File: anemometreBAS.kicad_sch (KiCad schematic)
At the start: 15 parts, among them U1 TP4056

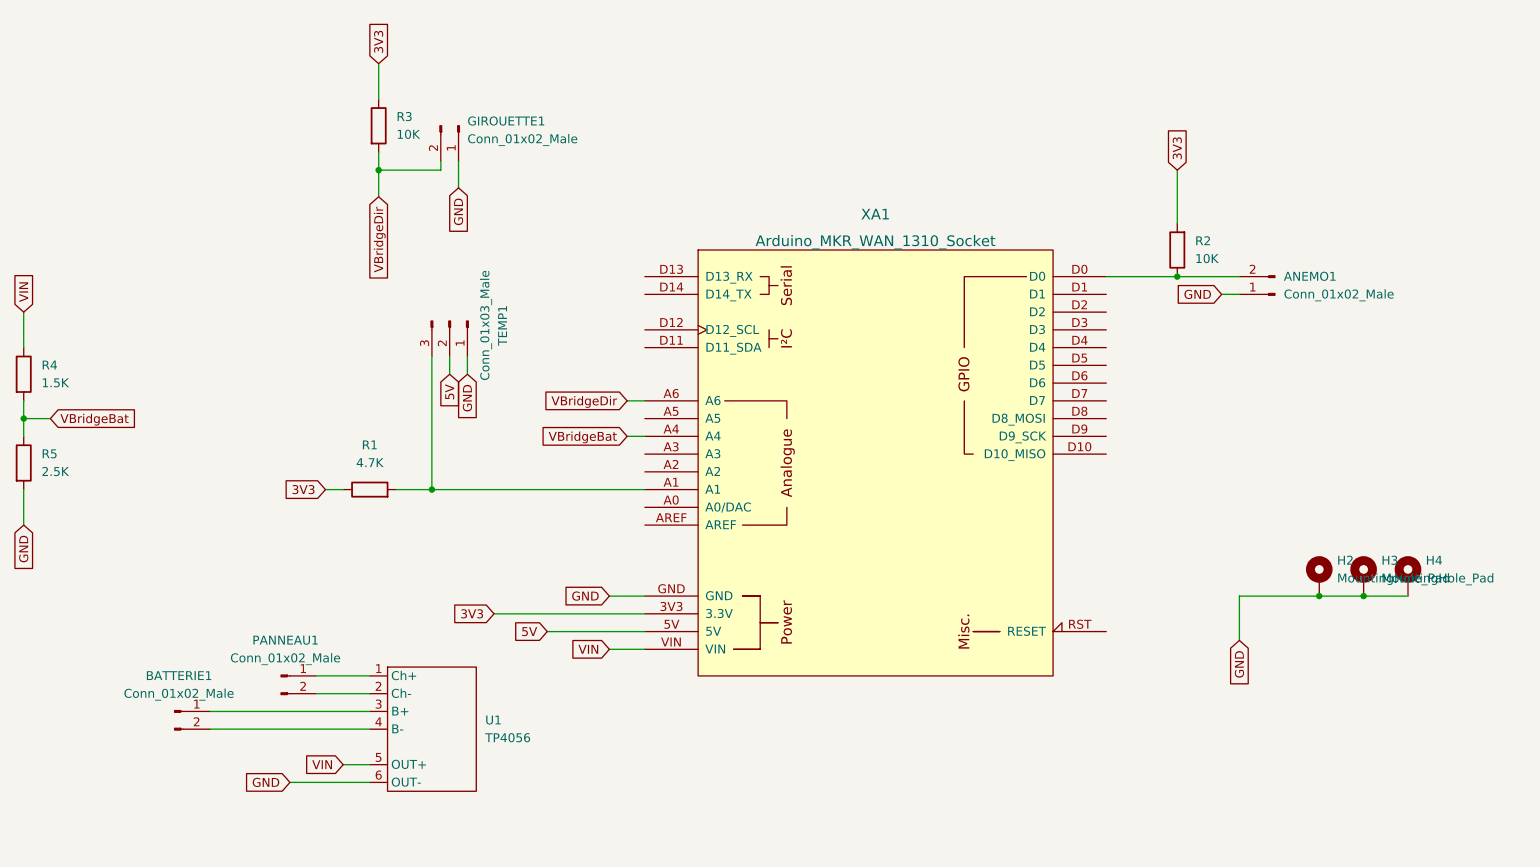
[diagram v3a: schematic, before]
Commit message: adding optionnal CEM schottky diode MKR 3D model update
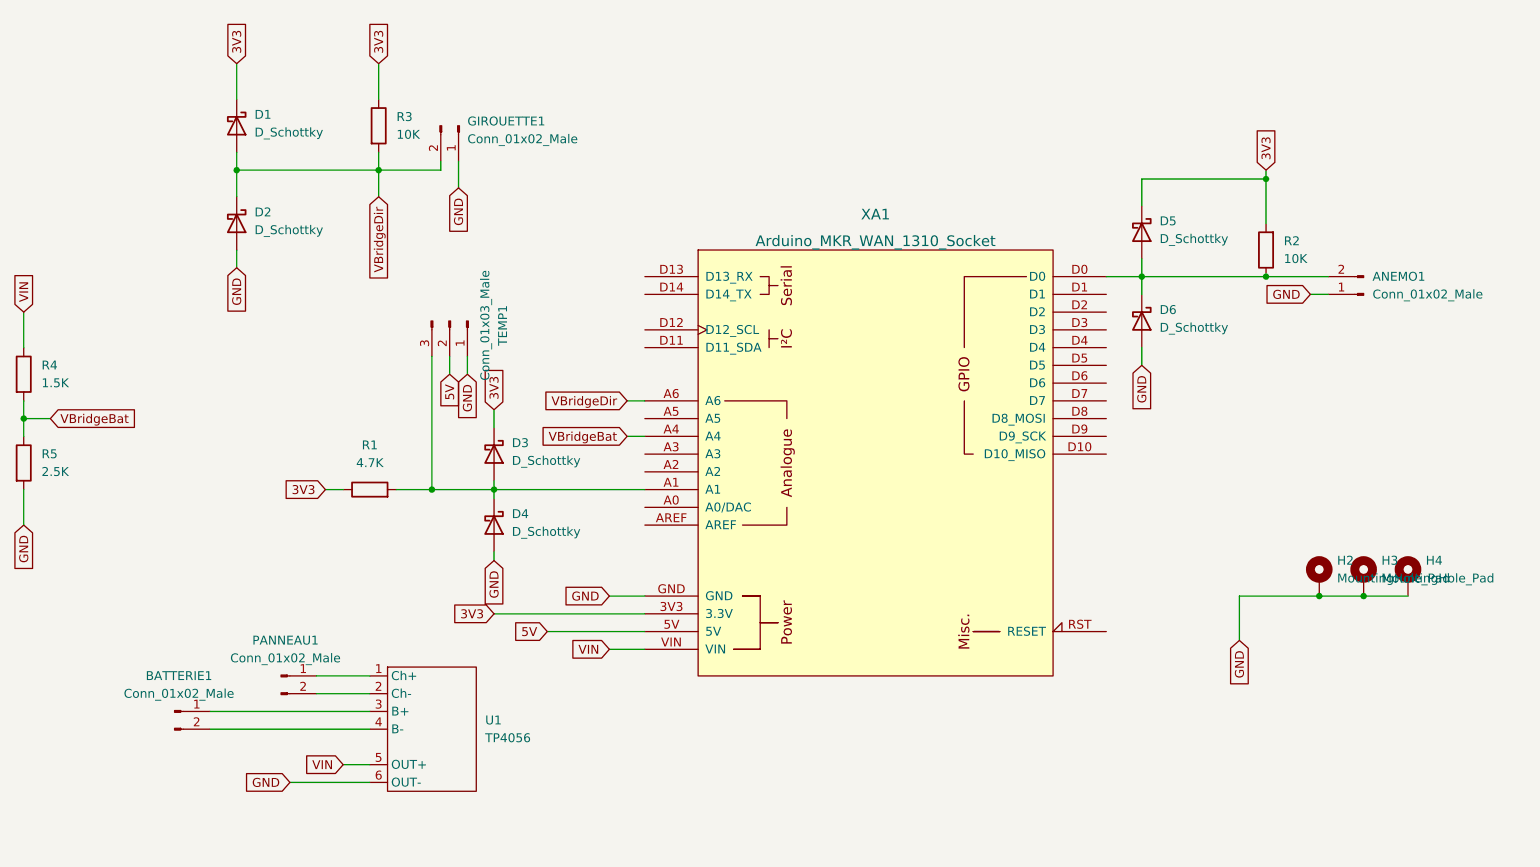
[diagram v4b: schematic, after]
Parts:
- added D1, D2, D3, D4, D5, D6: D_Schottky, Diode_THT:D_DO-35_SOD27_P7.62mm_Horizontal, symbol Device:D_Schottky
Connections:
- net 3V3: now also D1.1 (K), D3.1 (K), D5.1 (K)
- net GND: now also D2.2 (A), D4.2 (A), D6.2 (A)
- net VBridgeDir: now also D1.2 (A), D2.1 (K)
- net at R1.2, TEMP1.3 (Pin_3), XA1.A1: now also D3.2 (A), D4.1 (K)
- net at ANEMO1.2 (Pin_2), R2.1, XA1.D0: now also D5.2 (A), D6.1 (K)
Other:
- moved on the sheet: ANEMO1, R2

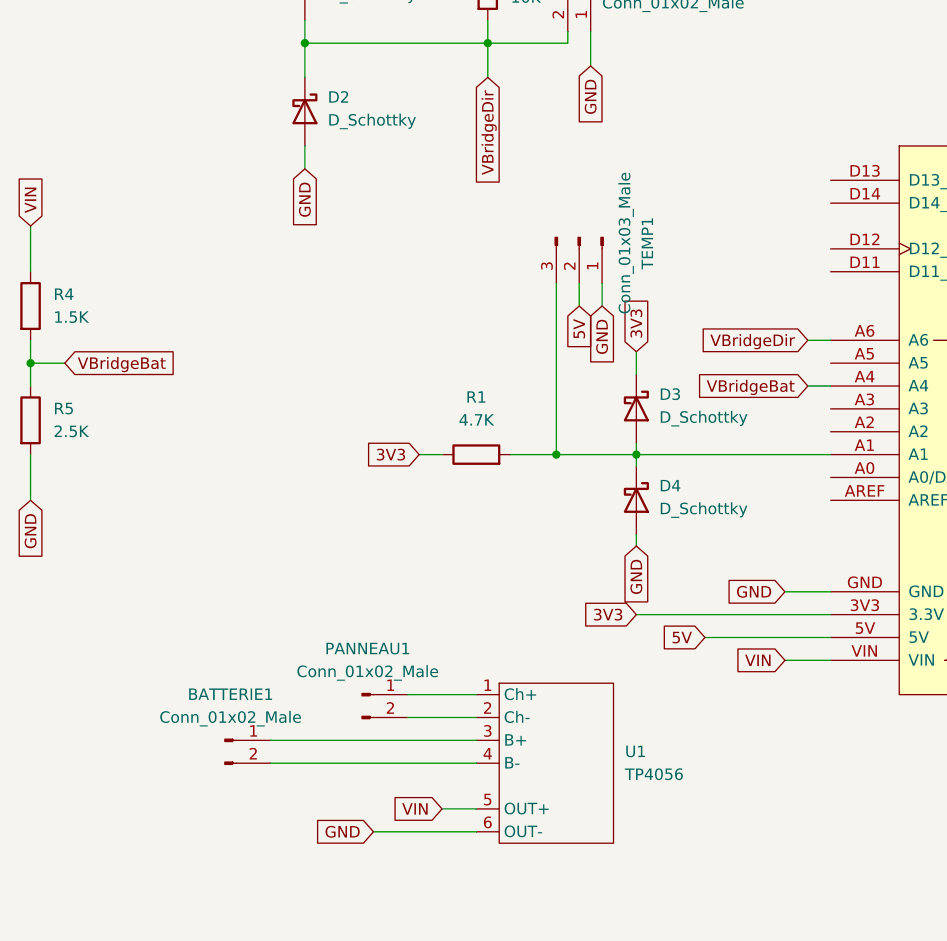
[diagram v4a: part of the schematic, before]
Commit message: Corrections alim (#2)
* Fix power issue

* add power connector as jst
routing pcb

---------

Co-authored-by: sdaviet <sylvain.daviet@gmail.com>
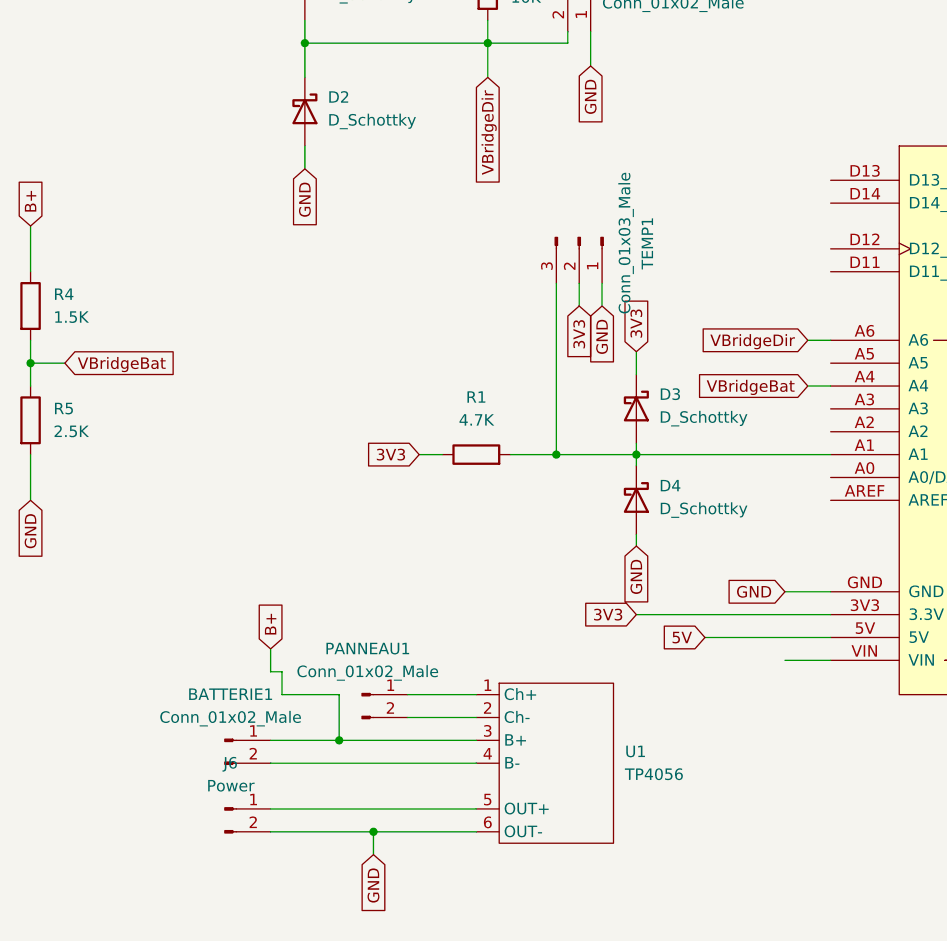
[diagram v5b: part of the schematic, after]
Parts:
- added J6: Power, Connector_JST:JST_XH_B2B-XH-A_1x02_P2.50mm_Vertical, symbol Connector:Conn_01x02_Male
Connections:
- net 3V3: now also TEMP1.2 (Pin_2)
- net 5V: no longer TEMP1.2 (Pin_2)
- net GND: now also J6.2 (Pin_2)
- net B+: now reaches BATTERIE1.1 (Pin_1), U1.3 (B+)
- net B+: now also R4.1
- removed net VIN: R4.1, U1.5 (OUT+), XA1.VIN
- new net: J6.1 (Pin_1), U1.5 (OUT+)
